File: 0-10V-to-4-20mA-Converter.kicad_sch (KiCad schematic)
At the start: 8 parts, among them J1 Conn_01x02_Pin, J2 Conn_01x02_Pin, J3 Conn_01x02_Pin, U1 LM358P

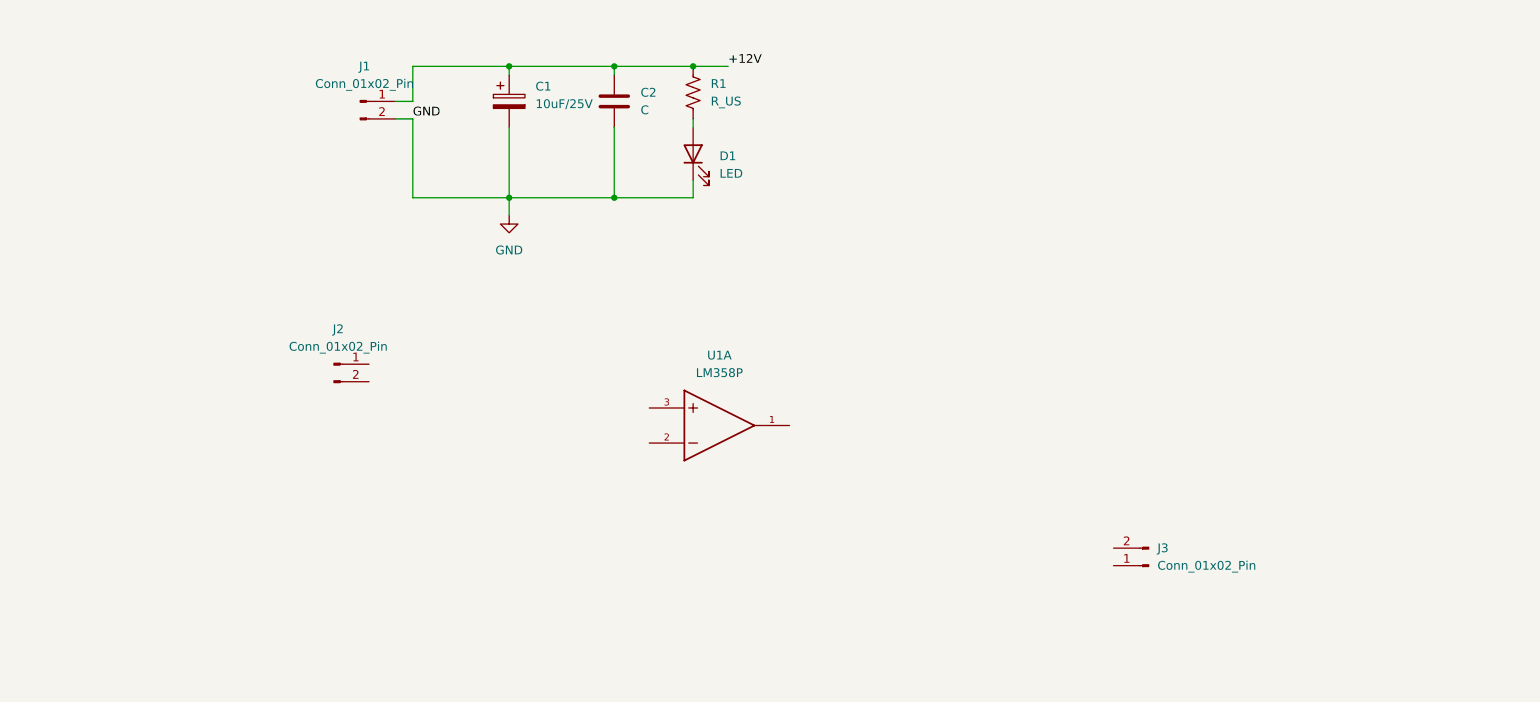
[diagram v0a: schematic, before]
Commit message: ERC and Schematic completed
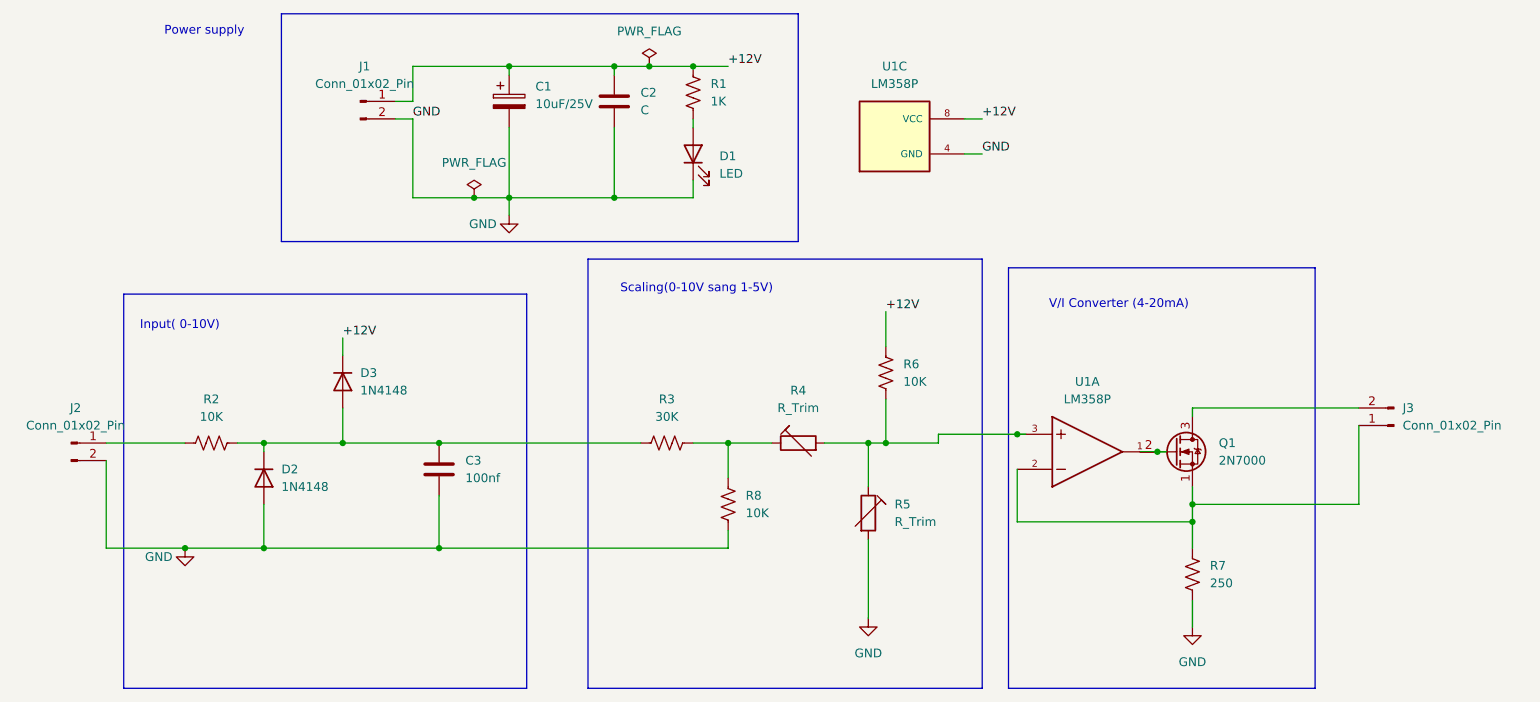
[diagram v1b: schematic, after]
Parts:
- added C3: 100nf, symbol Device:C
- added D2, D3: 1N4148, Diode_THT:D_DO-35_SOD27_P7.62mm_Horizontal, symbol Diode:1N4148
- added Q1: 2N7000, Package_TO_SOT_THT:TO-92_Inline, symbol Transistor_FET:2N7000
- added R2, R6, R8: 10K, symbol Device:R_US
- added R3: 30K, symbol Device:R_US
- added R4, R5: R_Trim, symbol Device:R_Trim
- added R7: 250, symbol Device:R_US
- added unit 3 of U1
- R1: value R_US -> 1K
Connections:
- net +12V: now also D3.1 (K), R6.1, U1.8 (VCC)
- net GND: now also J2.2 (Pin_2), C3.2, D2.2 (A), R5.2, R7.2, R8.2, U1.4 (GND)
- net at J2.1 (Pin_1): now also R2.1
- net at J3.1 (Pin_1): now also U1.2, Q1.1 (S), R7.1
- net at J3.2 (Pin_2): now also Q1.3 (D)
- net at U1.1: now also Q1.2 (G)
- net at U1.3: now also R4.2, R5.1, R6.2
- new net: C3.1, D2.1 (K), D3.2 (A), R2.2, R3.1
- new net: R3.2, R4.1, R8.1
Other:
- note added: "Input( 0-10V)"
- note added: "Power supply"
- note added: "Scaling(0-10V sang 1-5V)"
- note added: "V/I Converter (4-20mA)"
- moved on the sheet: J2, J3, U1A

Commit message: XTR116_replace
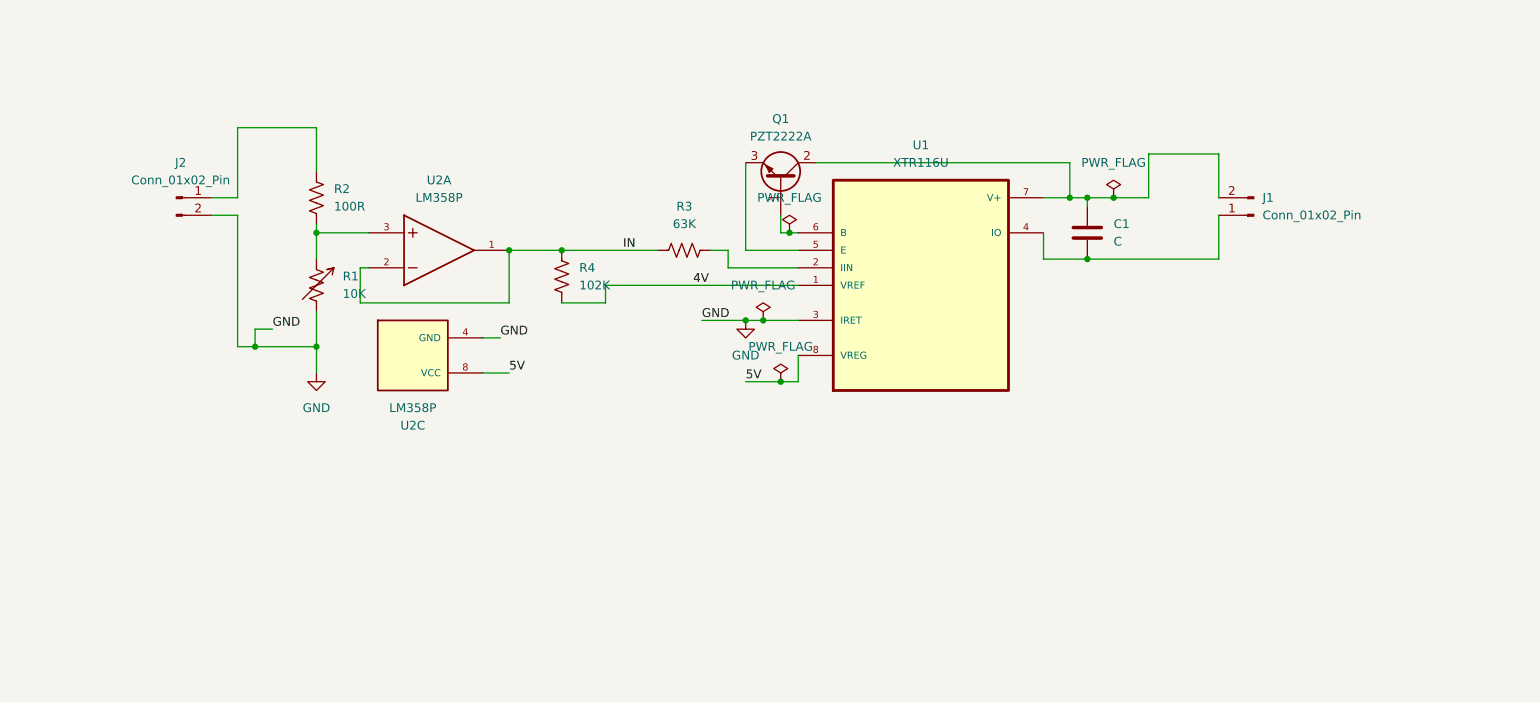
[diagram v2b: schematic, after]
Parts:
- removed C1: 10uF/25V, Capacitor_SMD:CP_Elec_4x5.4, symbol Device:C_Polarized
- removed C2: C, Capacitor_SMD:C_1210_3225Metric_Pad1.33x2.70mm_HandSolder, symbol Device:C
- removed C3: 100nf, symbol Device:C
- removed D1: LED, symbol Device:LED
- removed D2, D3: 1N4148, Diode_THT:D_DO-35_SOD27_P7.62mm_Horizontal, symbol Diode:1N4148
- removed J3: Conn_01x02_Pin, symbol Connector:Conn_01x02_Pin
- removed Q1: 2N7000, Package_TO_SOT_THT:TO-92_Inline, symbol Transistor_FET:2N7000
- removed R1: 1K, symbol Device:R_US
- removed R4, R5: R_Trim, symbol Device:R_Trim
- removed R6, R8: 10K, symbol Device:R_US
- removed R7: 250, symbol Device:R_US
- removed U1: LM358P, LM358P:DIP794W45P254L959H508Q8, symbol LM358P:LM358P
- added C1: C, symbol Device:C
- added Q1: PZT2222A, Package_TO_SOT_SMD:SOT-223-3_TabPin2, symbol Transistor_BJT:PZT2222A
- added R1: 10K, symbol Device:R_Variable_US
- added R4: 102K, symbol Device:R_US
- added U1: XTR116U, XTR116U:SOIC127P599X175-8N, symbol XTR116U:XTR116U
- added U2: LM358P, LM358P:DIP794W45P254L959H508Q8, symbol LM358P:LM358P
- R2: value 10K -> 100R
- R3: value 30K -> 63K
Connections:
- net GND: now also R1.2, U1.3 (IRET), U2.4 (GND); no longer J1.2 (Pin_2)
- net at R2.2: now also R1.1, U2.3; no longer R3.1
- net at R3.2: now also U1.2 (IIN)
- net +12V: no longer names the net of J1.1 (Pin_1)
- net +12V: now also C1.2, U1.4 (IO)
- new net: C1.1, J1.2 (Pin_2), Q1.2 (C), U1.7 (V+)
- new net: Q1.3 (E), U1.5 (E)
- new net: Q1.1 (B), U1.6 (B)
- new net 4V: R4.2, U1.1 (VREF)
- new net 5V: U1.8 (VREG), U2.8 (VCC)
- new net IN: R3.1, R4.1, U2.1, U2.2
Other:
- note removed: "Input( 0-10V)"
- note removed: "Power supply"
- note removed: "Scaling(0-10V sang 1-5V)"
- note removed: "V/I Converter (4-20mA)"

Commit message: XTR116 and MCP6002
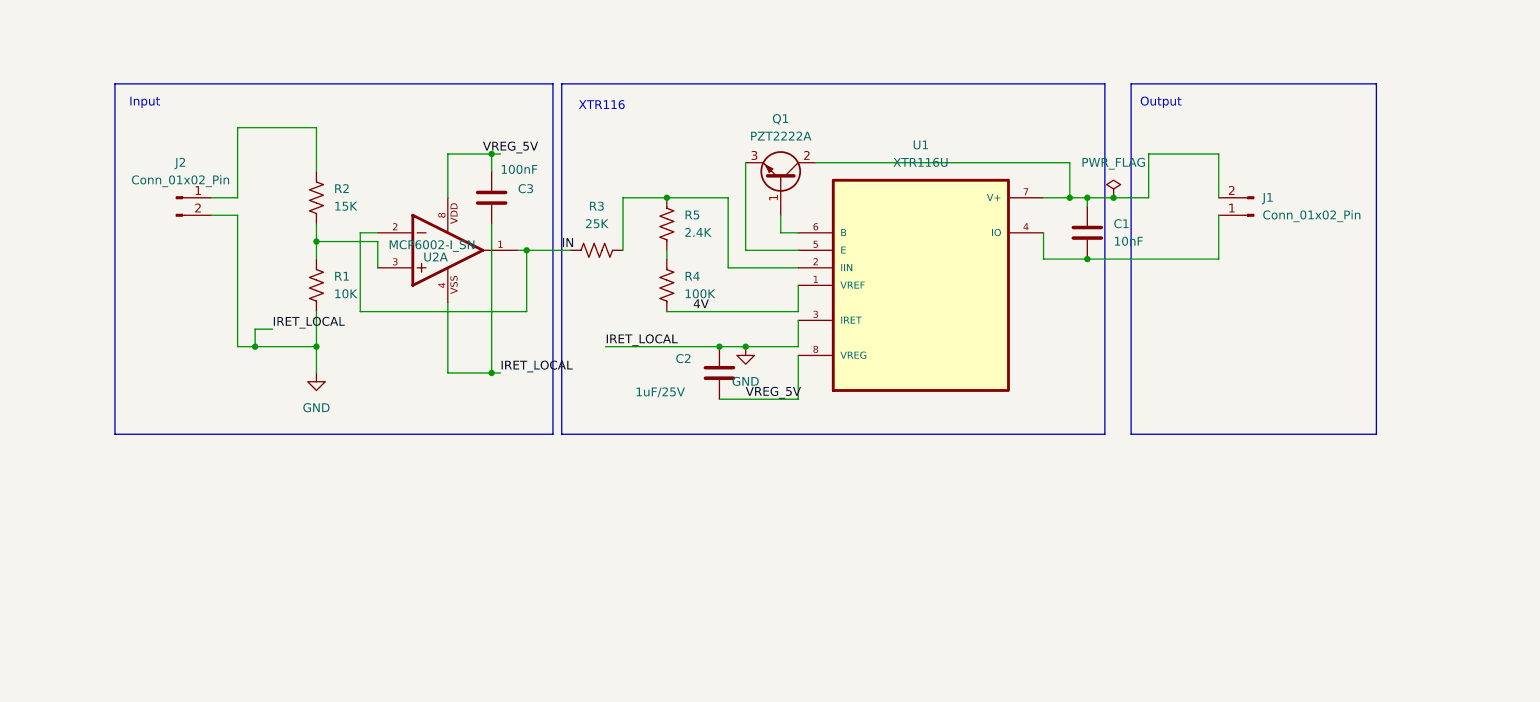
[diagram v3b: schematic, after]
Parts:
- removed R1: 10K, symbol Device:R_Variable_US
- removed U2: LM358P, LM358P:DIP794W45P254L959H508Q8, symbol LM358P:LM358P
- added C2: 1uF/25V, symbol Device:C
- added C3: 100nF, symbol Device:C
- added R1: 10K, symbol Device:R_US
- added R5: 2.4K, symbol Device:R_US
- added U2: MCP6002-I_SN, MCP6002-I_SN:SOIC127P600X175-8N, symbol MCP6002-I_SN:MCP6002-I_SN
- C1: value C -> 10nF
- R2: value 100R -> 15K
- R3: value 63K -> 25K
- R4: value 102K -> 100K
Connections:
- net GND: now also C2.1, C3.2, R1.2, U2.4
- net IN: now also U2.1, U2.2; no longer R4.1
- net at R3.2, U1.2 (IIN): now also R5.1
- net at R2.2: now also R1.1, U2.3
- net 5V renamed VREG_5V
- net VREG_5V: now also C2.2, C3.1, U2.8
- new net: R4.1, R5.2
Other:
- note added: "Input"
- note added: "Output"
- note added: "XTR116"
- moved on the sheet: R3, R4

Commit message: BP56-16 changed
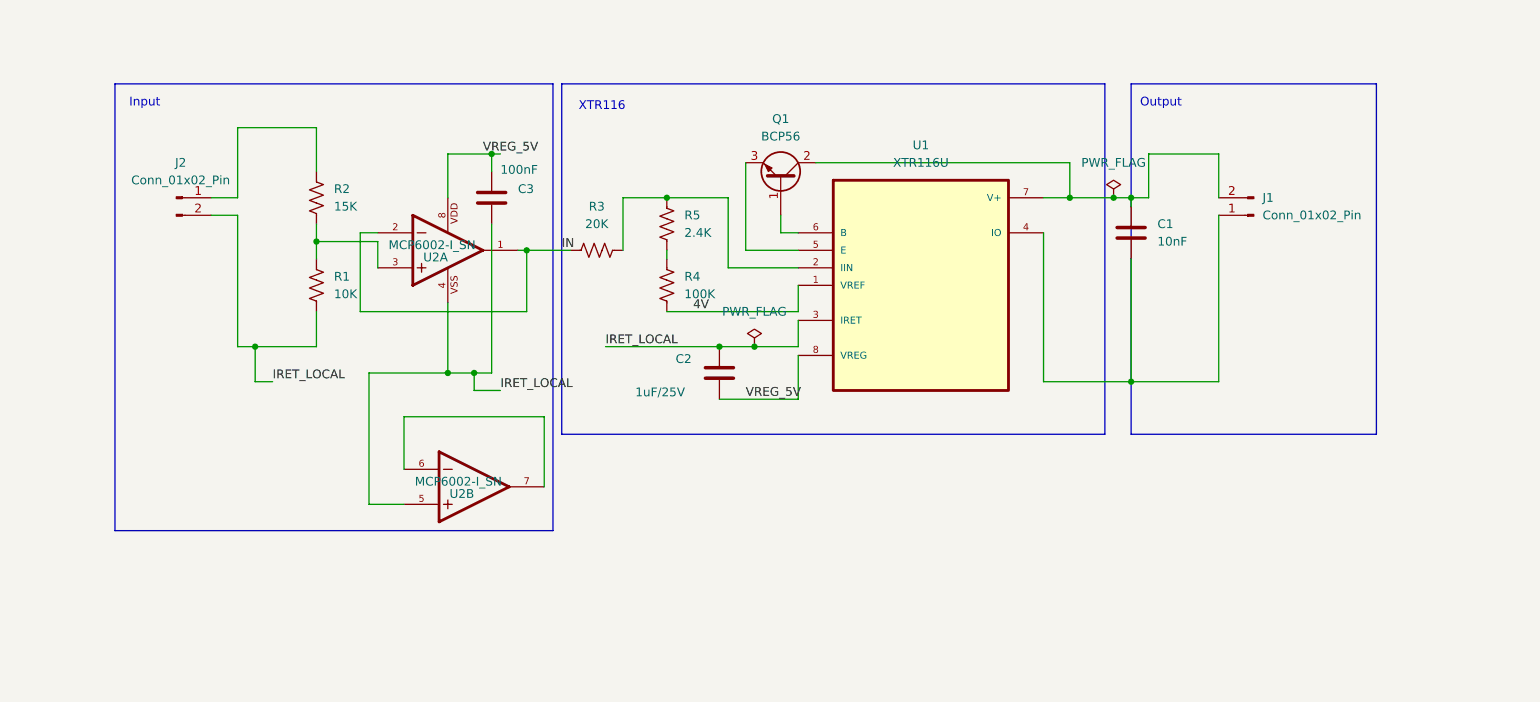
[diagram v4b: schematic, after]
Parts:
- removed Q1: PZT2222A, Package_TO_SOT_SMD:SOT-223-3_TabPin2, symbol Transistor_BJT:PZT2222A
- added Q1: BCP56, Package_TO_SOT_SMD:SOT-223-3_TabPin2, symbol Transistor_BJT:BCP56
- added unit 2 of U2
- C1, C2, C3: footprint (none) -> Capacitor_SMD:C_0805_2012Metric_Pad1.18x1.45mm_HandSolder
- J1, J2: footprint (none) -> TerminalBlock_Phoenix:TerminalBlock_Phoenix_MKDS-1,5-2-5.08_1x02_P5.08mm_Horizontal
- R1, R2, R4: footprint (none) -> Resistor_SMD:R_0805_2012Metric_Pad1.20x1.40mm_HandSolder
- R3: value 25K -> 20K; footprint (none) -> Resistor_SMD:R_0805_2012Metric_Pad1.20x1.40mm_HandSolder
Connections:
- net at C1.1, J1.2 (Pin_2), U1.7 (V+): now also Q1.2 (C), Q1.4 (C)
- net at U1.5 (E): now also Q1.3 (E)
- net at U1.6 (B): now also Q1.1 (B)
- net GND renamed IRET_LOCAL
- net IRET_LOCAL: now also U2.5
- new net: U2.6, U2.7
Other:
- moved on the sheet: C1

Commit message: Complete XTR116 PCB layout_DRC clean
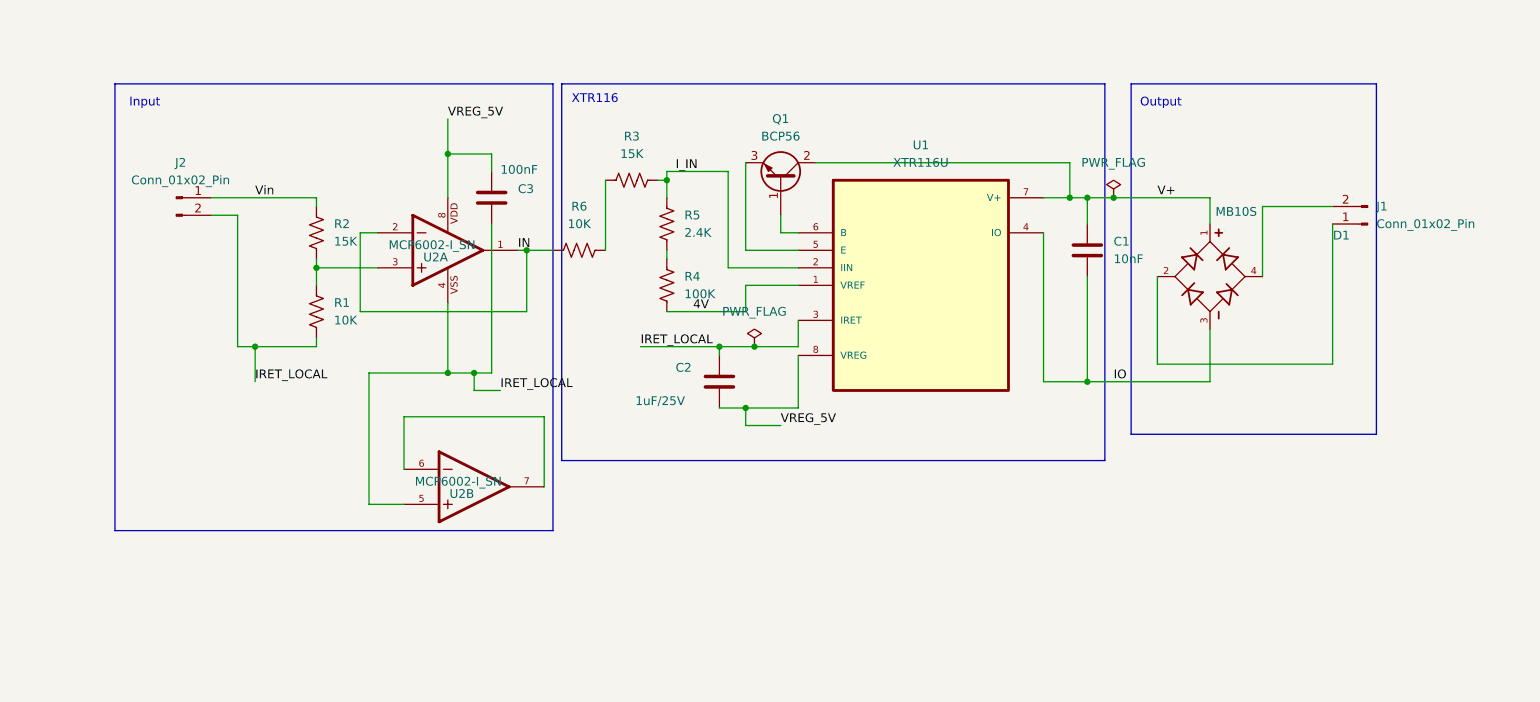
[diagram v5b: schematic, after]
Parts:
- added D1: MB10S, MB10S:MB10S_DiodesInc, symbol MB10S:MB10S
- added R6: 10K, Resistor_SMD:R_0805_2012Metric_Pad1.20x1.40mm_HandSolder, symbol Device:R_US
- J1, J2: footprint TerminalBlock_Phoenix:TerminalBlock_Phoenix_MKDS-1,5-2-5.08_1x02_P5.08mm_Horizontal -> XTR116_Final_Footprints_MB10S_KF301:KF301-2P_Universal_P5.08
- Q1: symbol Transistor_BJT:BCP56 -> Device:Q_NPN_BCE
- R3: value 20K -> 15K
- R5: footprint (none) -> Resistor_SMD:R_0805_2012Metric_Pad1.20x1.40mm_HandSolder
- U1: footprint XTR116U:SOIC127P599X175-8N -> Package_SO:SOIC-8_3.9x4.9mm_P1.27mm
- U2: footprint MCP6002-I_SN:SOIC127P600X175-8N -> Package_SO:SOIC-8_3.9x4.9mm_P1.27mm
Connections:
- net IN: now also R6.1; no longer R3.1
- net I_IN: now reaches R3.2, R5.1, U1.2 (IIN)
- net Vin: now reaches J2.1 (Pin_1), R2.1
- net V+: now reaches C1.1, Q1.2 (C), U1.7 (V+)
- net V+: now also D1.1; no longer J1.2 (Pin_2), Q1.4 (C)
- net IO: now reaches C1.2, U1.4 (IO)
- net IO: now also D1.3; no longer J1.1 (Pin_1)
- new net: R3.1, R6.2
- new net: D1.2, J1.1 (Pin_1)
- new net: D1.4, J1.2 (Pin_2)
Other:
- moved on the sheet: C2, J1, R1, R2, R3
